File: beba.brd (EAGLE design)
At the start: 65 x 30 mm, 37 parts, among them IC1 LT1302SO08, IC2 MCP73871-2AAI/ML

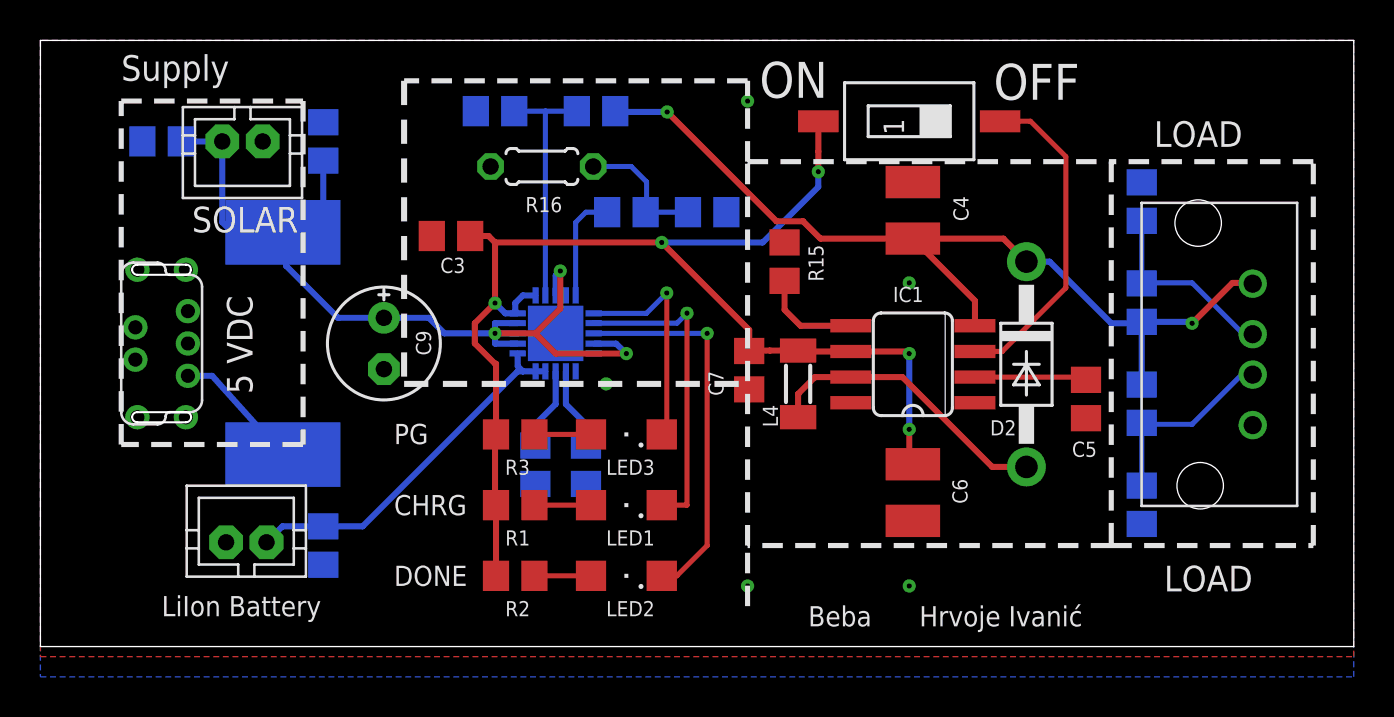
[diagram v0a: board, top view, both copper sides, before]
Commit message: - corrected issues with component placement, power inductor footprint, etc.
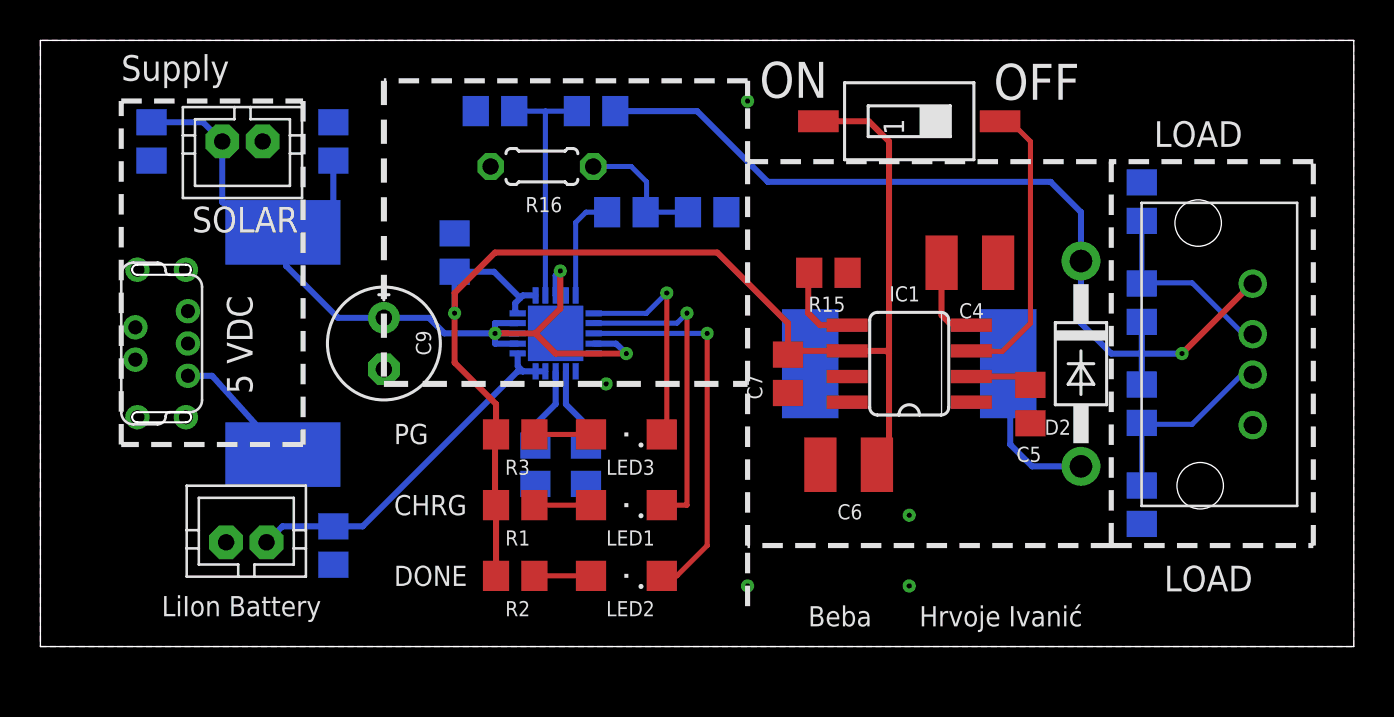
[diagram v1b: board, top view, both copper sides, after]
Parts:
- removed L4: DE1205-18, inductor-neosid:SM-1206
- added L: DE1205-18, DE1205-18 Power Inductor:SMT
- moved C4 3.83 mm to (46.0, 19.0), turned to 180 degrees
- moved C6 3.47 mm to (40.0, 9.00), turned to 0 degrees
- moved C5 2.76 mm to (49.0, 12.0)
- moved D2 2.70 mm to (51.5, 14.0)
- moved R15 2.24 mm to (39.0, 18.5), turned to 0 degrees
- moved C7 1.93 mm to (37.0, 13.5)
- moved C3 0.84 mm to (20.5, 19.5), flipped to the bottom, turned to 90 degrees
- moved C1 0.50 mm to (14.5, 5.00)
- moved C2 0.50 mm to (5.50, 25.0), turned to 270 degrees
- moved C8 0.50 mm to (14.5, 25.0)
- moved IC1 0.18 mm to (43.0, 14.0)
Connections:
- new net N$4: D2.A, L.L1
- net SW: no longer D2.A, L4.1
- net V_LIION_REGULATED: now also L.L2; no longer L4.2
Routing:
- net SW: track 14.6 -> 0.00 mm
- net N$4: track 0.00 -> 8.12 mm
- net V_LIION_REGULATED: track 62.9 -> 68.0 mm, vias 5 -> 1
- net VCC: track 45.5 -> 48.7 mm, vias 2 -> 1
- net 5V0: track 46.4 -> 48.9 mm
- net VC: track 5.55 -> 3.10 mm
- net SHDN: track 16.3 -> 14.4 mm
- net IT: track 5.04 -> 4.19 mm
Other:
- board text added: "+"
- board text added: "-"

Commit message: - further minor corrections
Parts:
- added 5V0, VLIION: PTR1B2,54, testpad:B2,54
- moved S1 2.06 mm to (45.0, 25.5)
- moved C1 0.71 mm to (14.0, 4.50)
- moved C2 0.71 mm to (5.00, 24.5)
- moved C3 0.71 mm to (20.0, 19.0)
- moved C4 0.71 mm to (45.5, 18.5)
- moved C5 0.71 mm to (48.5, 11.5)
- moved C6 0.71 mm to (39.5, 8.50)
- moved C7 0.71 mm to (36.5, 13.0)
- moved C8 0.71 mm to (14.0, 24.5)
- moved C9 0.71 mm to (16.5, 14.5)
- moved CONN1 0.71 mm to (5.50, 14.5)
- moved CONN2 0.71 mm to (9.69, 4.66)
- moved CONN3 0.71 mm to (9.50, 24.5)
- moved CONN4 0.71 mm to (59.5, 14.0)
- moved D2 0.71 mm to (51.0, 13.5)
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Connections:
- net 5V0: now also 5V0.TP
- net V_LIION_REGULATED: now also VLIION.TP
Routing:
- net 5V0: track 48.9 -> 61.6 mm
- net VCC: track 48.7 -> 52.8 mm, vias 1 -> 2
- net V_LIION_REGULATED: track 68.0 -> 69.1 mm
- net SHDN: track 14.4 -> 13.9 mm
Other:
- board size 65 x 30 mm -> 64 x 29.5 mm
- board text added: "Solar"
- board text removed: "SOLAR"

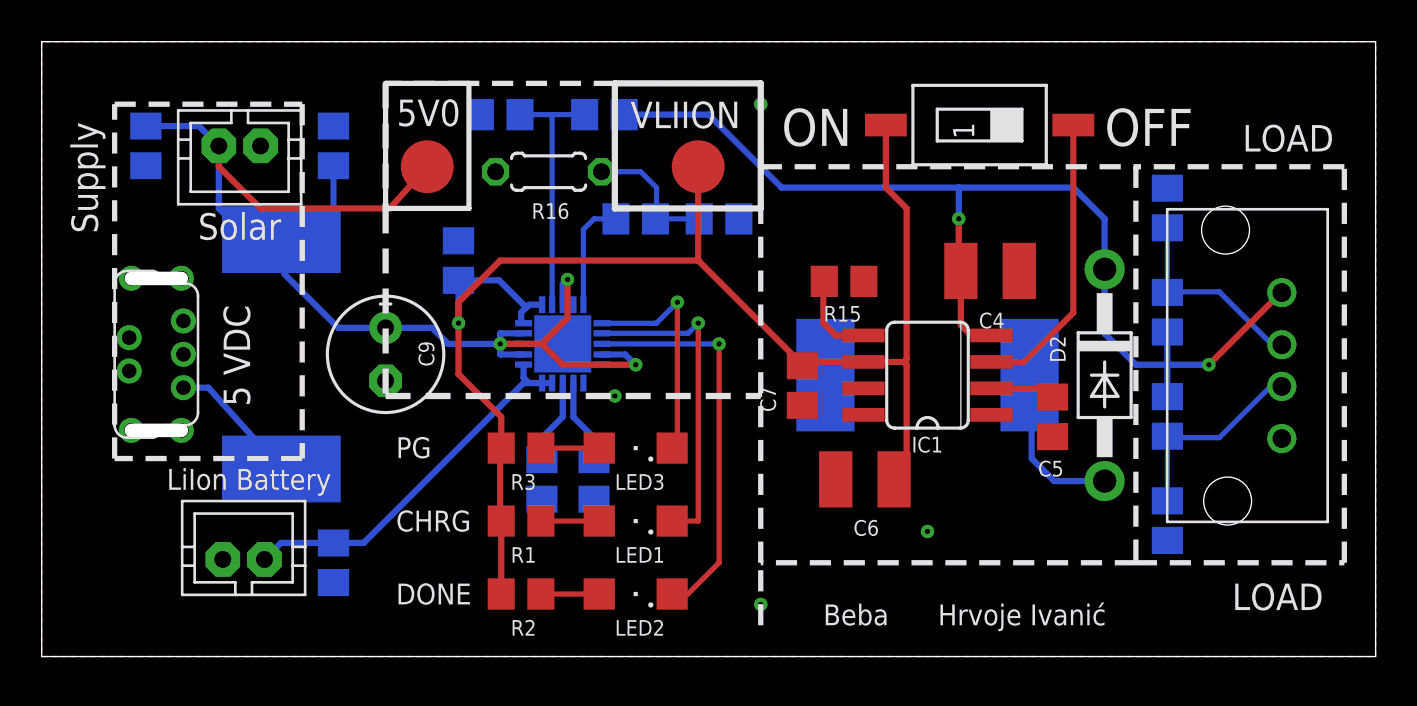
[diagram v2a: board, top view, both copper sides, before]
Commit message: - minor corrections, added bom
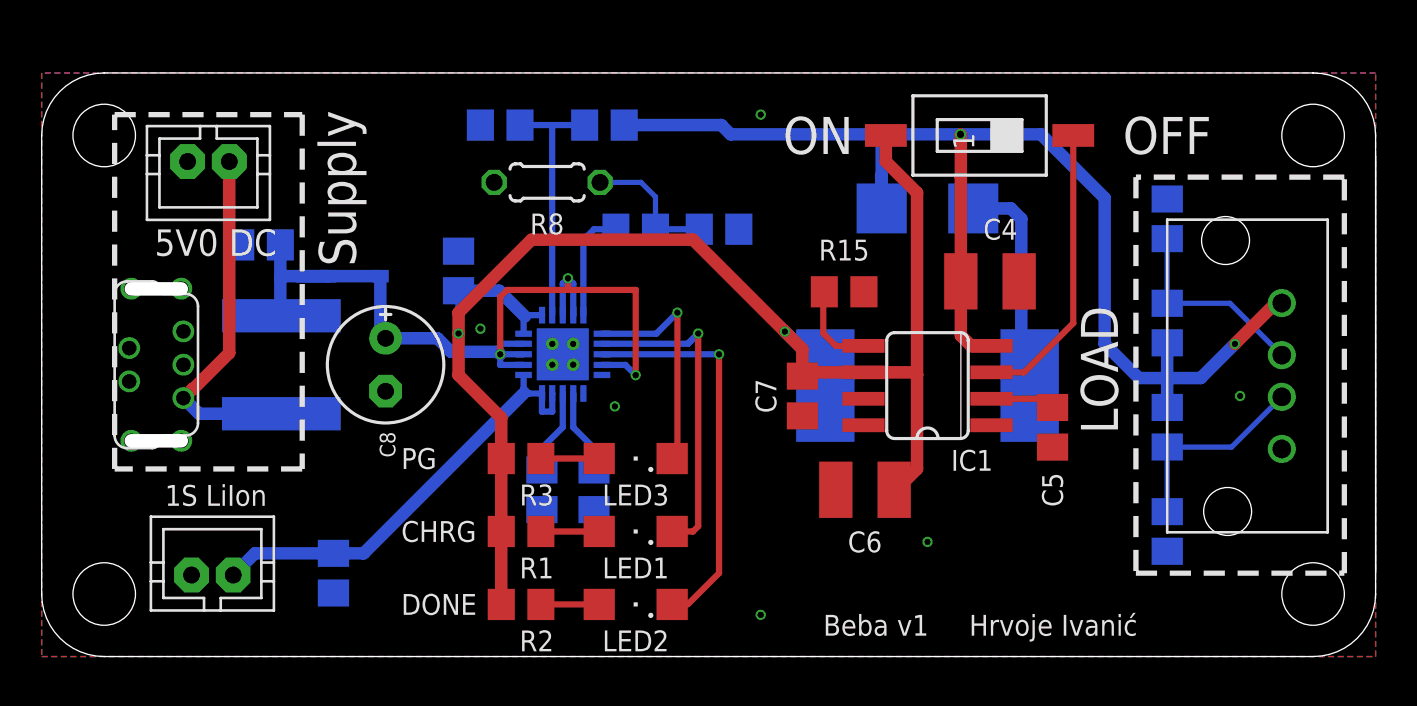
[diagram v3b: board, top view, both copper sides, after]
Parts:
- removed 5V0, VLIION: PTR1B2,54, testpad:B2,54
- removed C9: 4700μF / 10V, rcl:E2,5-6E
- removed L: DE1205-18, DE1205-18 Power Inductor:SMT
- removed R16: NTC - 10k, resistor:0204/5
- added D1: BAT60J, diode:SOD323_ST
- added L2: DE1205-18, DE1205-18 Power Inductor:SMT
- added R8: NTC - 10k, resistor:0204/5
- C8: value 10μF -> 4700μF / 10V; device resistor:C0805 -> rcl:E2,5-6E
- D2: value 1N4148 -> MBRS130LT3; device adafruit:DO41-10 -> diode:SMB
- IC2: device Microchip-MCP73871-2AAI_ML:QFN50P400X400X100-21N -> MCP73871 - Powerpath and Charge Controller:QFN50P400X400X100-21N
- moved D2 11.7 mm to (42.5, 21.5), flipped to the bottom, turned to 180 degrees
- moved C8 10.8 mm to (16.5, 14.0), flipped to the top, turned to 270 degrees
- moved C2 7.27 mm to (10.5, 19.8), turned to 0 degrees
- moved CONN2 1.68 mm to (8.19, 3.91)
- moved CONN3 1.68 mm to (8.00, 23.8)
- moved R11 0.52 mm to (54.0, 16.0)
- moved R12 0.52 mm to (54.0, 21.0)
- moved R13 0.52 mm to (54.0, 11.0)
- moved R14 0.52 mm to (54.0, 6.00)
- moved C1 0.50 mm to (14.0, 4.00)
- moved C3 0.50 mm to (20.0, 18.5)
- moved C4 0.50 mm to (45.5, 18.0)
- moved C5 0.50 mm to (48.5, 11.0)
- moved C6 0.50 mm to (39.5, 8.00)
- moved C7 0.50 mm to (36.5, 12.5)
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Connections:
- net 5V0: now also C8.+, D1.A, D1.C, IC2.17_CE, IC2.18_IN1, IC2.19_IN2, IC2.3_SEL, IC2.4_PROG2, IC2.9_!TE!, L1.1; no longer 5V0.TP, C8.1, C9.+, CONN3.1, IC2.17, IC2.18, IC2.19, IC2.3, IC2.4, IC2.9, L1.P$1
- net GND: now also C8.-, CONN3.1, IC2.10_GND1, IC2.11_GND2, IC2.GND2, IC2.GND3, IC2.GND4, IC2.GND5, IC2.GND6, R8.2; no longer C8.2, C9.-, CONN3.2, IC2.10, IC2.11, R16.2
- net N$10: now also R8.1; no longer R16.1
- net N$4: now also L2.L1; no longer L.L1
- net PG: now also IC2.!6_PG!; no longer IC2.6
- net PROG1: now also IC2.13_PROG1; no longer IC2.13
- net PROG3: now also IC2.12_PROG3; no longer IC2.12
- net STAT1: now also IC2.8_STAT1; no longer IC2.8
- net STAT2: now also IC2.7_STAT2; no longer IC2.7
- net THERM: now also IC2.5_THERM; no longer IC2.5
- net VPCC: now also IC2.2_VPCC; no longer IC2.2
- net VUSB: now also CONN3.2, L1.2; no longer L1.P$2
- net V_LIION+: now also IC2.14_VBAT1, IC2.15_VBAT2, IC2.16_BAT_SENSE; no longer IC2.14, IC2.15, IC2.16
- net V_LIION_REGULATED: now also IC2.1_OUT1, IC2.20_OUT2, L2.L2; no longer IC2.1, IC2.20, L.L2, VLIION.TP
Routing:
- net 5V0: track 61.6 -> 42.7 mm
- net VUSB: track 7.12 -> 17.3 mm
- net VCC: track 52.8 -> 62.0 mm
- net V_LIION+: track 18.3 -> 21.7 mm
- net N$4: track 8.12 -> 10.7 mm
- net V_LIION_REGULATED: track 69.1 -> 71.6 mm, vias 1 -> 2
- net GND: track 0.00 -> 0.71 mm, vias 4 -> 6
- net STAT2: track 15.6 -> 16.1 mm
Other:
- board size 64 x 29.5 mm -> 64 x 28 mm
- board text added: "1S LiIon"
- board text added: "5V0 DC"
- board text added: "Beba v1"
- board text removed: "+"
- board text removed: "-"
- board text removed: "5 VDC"
- board text removed: "Beba"
- board text removed: "LiIon Battery"
- board text removed: "Solar"

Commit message: - rewrote schematic into sheets
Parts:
- removed C1: 10uF, resistor:C0805
- removed C2, C3, C5: 10μF, resistor:C0805
- removed C4, C6: 220μF, resistor:C1210
- removed C7: 0.1μF, resistor:C0805
- removed C8: 4700μF / 10V, rcl:E2,5-6E
- removed CONN1: MX500075-1517USB_MINI-B, MX500075-1517 USB Mini-B straight socket:TH
- removed CONN2: LiIon, jst-ph:JST-PH2
- removed CONN3: 5VDC, jst-ph:JST-PH2
- removed CONN4: USB-A female socket, right angle, 1734366-1 USB-A socket, vertical:TH
- removed D1: BAT60J, diode:SOD323_ST
- removed D2: MBRS130LT3, diode:SMB
- removed IC1: LT1302SO08, adafruit:SO08
- removed IC2: MCP73871-2AAI/ML, MCP73871 - Powerpath and Charge Controller:QFN50P400X400X100-21N
- removed L1: DJNR6045-100-S, DJNR6045-100S Power Inductor:DJNR6045-100-S
- removed L2: DE1205-18, DE1205-18 Power Inductor:SMT
- removed LED1: green, led:SML1206
- removed LED2: orange, led:SML1206
- removed LED3: red, led:SML1206
- removed R10, R5: 100k, resistor:R0805
- removed R11, R13: 75k, resistor:R0805
- removed R12, R14: 49k9, resistor:R0805
- removed R15: 270k, resistor:R0805
- removed R6, R9: 1k, resistor:R0805
- removed R7: 150k, resistor:R0805
- removed R8: NTC - 10k, resistor:0204/5
- removed S1: POWER, smd-special:SMS-001
- added CN1, CN2, CN3: S2B-PH-K-S, adafruit:JST-PH-2-THM-RA
- added IDEAL_DIODE1:C1, IDEAL_DIODE2:C1, IDEAL_DIODE3:C1, TPS630701-1:C11: 0.1μF, rcl:C0805
- added IDEAL_DIODE1:IC1, IDEAL_DIODE2:IC1, IDEAL_DIODE3:IC1: SIA456DJ-T1-GE3, SIA456DJ-T1-GE3 N-Fet:SC-70-6
- added IDEAL_DIODE1:IC2, IDEAL_DIODE2:IC2, IDEAL_DIODE3:IC2: LM74670QDGKTQ1, LM74670 - Smart Diode Rectifier Controller:VSSOP-8
- added MCP73871-1:C16: 4700μF / 10V, C-Pol:TH
- added MCP73871-1:C4: 10μF, resistor:C0805
- added MCP73871-1:C6, MCP73871-1:C7: 10u, resistor:C0805
- added MCP73871-1:IC7: (no value), MCP73871 - Powerpath and Charge Controller:QFN50P400X400X100-21N
- added MCP73871-1:LED1: LTST-C230KRKT - red, led:SML1206
- added MCP73871-1:LED2: LTST-C230KGKT - green, led:SML1206
- added MCP73871-1:LED3: LTST-C230KSKT - yellow, led:SML1206
- added MCP73871-1:R1, MCP73871-1:R2, MCP73871-1:R3, MCP73871-1:R6, MCP73871-1:R7: 1k, resistor:R0805
- added MCP73871-1:R10: NTC - 10k, resistor:0204/5
- added MCP73871-1:R4: 270k, resistor:R0805
- added MCP73871-1:R5, MCP73871-1:R8: 100k, resistor:R0805
- added MCP73871-1:R9: 150k, resistor:R0805
- added TPS630701-1:C10, TPS630701-1:C12, TPS630701-1:C8, TPS630701-1:C9: 10u, rcl:C0805
- added TPS630701-1:C13, TPS630701-1:C14, TPS630701-1:C15: 22u, rcl:C0805
- added TPS630701-1:IC8: TPS630701, TPS630701 - Buck Boost 5V regulator:VQFN
- added TPS630701-1:L1: XFL4020-152MEB, XFL4020-152MEC Inductor 1.5uH:SMD
- added TPS630701-1:R11: 100k, rcl:R0805
- added TPS630701-1:R12: 10k, rcl:R0805
- added USB-B1: 67503-1230, MX-67503-1230 USB Mini-B SMT straight socket:SMT
- added X1: 62900416021, con-yamaichi:USB-A003
- R1, R3: value 1k -> 75k
- R2: value 1k -> 49k9
- R4: value 270k -> 49k9
- moved R4 252.9 mm to (-95.0, -196.0), flipped to the top, turned to 0 degrees
- moved R3 243.6 mm to (-96.0, -203.0)
- moved R1 243.0 mm to (-101.0, -203.0)
- moved R2 234.0 mm to (-101.0, -196.0)
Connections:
- removed net 5V0: C2.1, C8.+, D1.A, D1.C, IC2.17_CE, IC2.18_IN1, IC2.19_IN2, IC2.3_SEL, IC2.4_PROG2, IC2.9_!TE!, L1.1
- removed net IT: IC1.5, R15.1
- removed net N$1: LED3.A, R3.2
- removed net N$10: R6.2, R7.1, R8.1
- removed net N$2: LED2.A, R2.2
- removed net N$3: LED1.A, R1.2
- removed net N$4: D2.A, L2.L1
- removed net PG: IC2.!6_PG!, LED3.C
- removed net PROG1: IC2.13_PROG1, R9.1
- removed net PROG3: IC2.12_PROG3, R10.1
- removed net SHDN: IC1.3, S1.2
- removed net STAT1: IC2.8_STAT1, LED2.C
- removed net STAT2: IC2.7_STAT2, LED1.C
- removed net SW: IC1.7
- removed net THERM: IC2.5_THERM, R6.1
- removed net VC: C5.2, IC1.2
- removed net VCC: C4.2, CONN4.VCC, D2.C, IC1.4, R11.2, R13.2, R4.2
- removed net VPCC: IC2.2_VPCC, R4.1, R5.2
- removed net VUSB: CONN1.VBUS, CONN3.2, L1.2
- new net 5V0_IN: IDEAL_DIODE1:IC1.1_D, IDEAL_DIODE1:IC1.2_D, IDEAL_DIODE1:IC1.5_D, IDEAL_DIODE1:IC1.6_D, IDEAL_DIODE1:IC1.8_D, IDEAL_DIODE1:IC2.CATHODE, IDEAL_DIODE2:IC1.1_D, IDEAL_DIODE2:IC1.2_D, IDEAL_DIODE2:IC1.5_D, IDEAL_DIODE2:IC1.6_D, IDEAL_DIODE2:IC1.8_D, IDEAL_DIODE2:IC2.CATHODE, IDEAL_DIODE3:IC1.1_D, IDEAL_DIODE3:IC1.2_D, IDEAL_DIODE3:IC1.5_D, IDEAL_DIODE3:IC1.6_D, IDEAL_DIODE3:IC1.8_D, IDEAL_DIODE3:IC2.CATHODE
- new net 5V0_OUT: R1.2, R3.2, X1.1
- new net IDEAL_DIODE1:GATE_DRIVER: IDEAL_DIODE1:IC1.3_G, IDEAL_DIODE1:IC2.GATE_DRIVE, IDEAL_DIODE1:IC2.GATE_PULLD
- new net IDEAL_DIODE1:VCAPH: IDEAL_DIODE1:C1.2, IDEAL_DIODE1:IC2.VCAPH
- new net IDEAL_DIODE1:VCAPL: IDEAL_DIODE1:C1.1, IDEAL_DIODE1:IC2.VCAPL
- new net IDEAL_DIODE2:GATE_DRIVER: IDEAL_DIODE2:IC1.3_G, IDEAL_DIODE2:IC2.GATE_DRIVE, IDEAL_DIODE2:IC2.GATE_PULLD
- new net IDEAL_DIODE2:VCAPH: IDEAL_DIODE2:C1.2, IDEAL_DIODE2:IC2.VCAPH
- new net IDEAL_DIODE2:VCAPL: IDEAL_DIODE2:C1.1, IDEAL_DIODE2:IC2.VCAPL
- new net IDEAL_DIODE3:GATE_DRIVER: IDEAL_DIODE3:IC1.3_G, IDEAL_DIODE3:IC2.GATE_DRIVE, IDEAL_DIODE3:IC2.GATE_PULLD
- new net IDEAL_DIODE3:VCAPH: IDEAL_DIODE3:C1.2, IDEAL_DIODE3:IC2.VCAPH
- new net IDEAL_DIODE3:VCAPL: IDEAL_DIODE3:C1.1, IDEAL_DIODE3:IC2.VCAPL
- new net MCP73871-1:5V0_IN: MCP73871-1:C16.POS, MCP73871-1:C4.1, MCP73871-1:IC7.17_CE, MCP73871-1:IC7.18_IN1, MCP73871-1:IC7.19_IN2, MCP73871-1:IC7.3_SEL, MCP73871-1:IC7.4_PROG2, MCP73871-1:IC7.9_!TE!, MCP73871-1:R1.1, MCP73871-1:R2.1, MCP73871-1:R3.1, MCP73871-1:R4.2
- new net MCP73871-1:LED1_A: MCP73871-1:LED1.A, MCP73871-1:R1.2
- new net MCP73871-1:LED2_A: MCP73871-1:LED2.A, MCP73871-1:R2.2
- new net MCP73871-1:LED3_A: MCP73871-1:LED3.A, MCP73871-1:R3.2
- new net MCP73871-1:N$10: MCP73871-1:R10.1, MCP73871-1:R6.2, MCP73871-1:R9.1
- new net MCP73871-1:PG: MCP73871-1:IC7.!6_PG!, MCP73871-1:LED1.C
- new net MCP73871-1:PROG1: MCP73871-1:IC7.13_PROG1, MCP73871-1:R7.1
- new net MCP73871-1:PROG3: MCP73871-1:IC7.12_PROG3, MCP73871-1:R8.1
- new net MCP73871-1:STAT1: MCP73871-1:IC7.8_STAT1/!LBO!, MCP73871-1:LED3.C
- new net MCP73871-1:STAT2: MCP73871-1:IC7.7_STAT2, MCP73871-1:LED2.C
- new net MCP73871-1:THERM: MCP73871-1:IC7.5_THERM, MCP73871-1:R6.1
- new net MCP73871-1:VPCC: MCP73871-1:IC7.2_VPCC, MCP73871-1:R4.1, MCP73871-1:R5.2
- new net MCP73871-1:V_LIION+: MCP73871-1:C7.1, MCP73871-1:IC7.14_VBAT1, MCP73871-1:IC7.15_VBAT2, MCP73871-1:IC7.16_BAT_SENSE
- new net MCP73871-1:V_LIION_REGULATED: MCP73871-1:C6.1, MCP73871-1:IC7.1_OUT1, MCP73871-1:IC7.20_OUT2
- new net TPS630701-1:5V0_OUT: TPS630701-1:C12.2, TPS630701-1:C13.2, TPS630701-1:C14.2, TPS630701-1:C15.2, TPS630701-1:IC8.5-FB, TPS630701-1:IC8.7-VOUT, TPS630701-1:IC8.8-VOUT, TPS630701-1:IC8.VOUT, TPS630701-1:R11.2
- new net TPS630701-1:L1: TPS630701-1:IC8.11-L1, TPS630701-1:L1.P$1
- new net TPS630701-1:L2: TPS630701-1:IC8.9-L2, TPS630701-1:L1.P$2
- new net TPS630701-1:N$8: TPS630701-1:IC8.1-PS/S, TPS630701-1:IC8.14-EN, TPS630701-1:R12.1
- new net TPS630701-1:PG1: TPS630701-1:IC8.2-PG, TPS630701-1:R11.1
- new net TPS630701-1:VAUX: TPS630701-1:C11.2, TPS630701-1:IC8.3-VAUX
- new net VINPUT1: CN1.1, IDEAL_DIODE2:IC1.4_S, IDEAL_DIODE2:IC1.7_S, IDEAL_DIODE2:IC2.ANODE
- new net VINPUT2: CN2.1, IDEAL_DIODE3:IC1.4_S, IDEAL_DIODE3:IC1.7_S, IDEAL_DIODE3:IC2.ANODE
- new net VUSB_MINI-B: IDEAL_DIODE1:IC1.4_S, IDEAL_DIODE1:IC1.7_S, IDEAL_DIODE1:IC2.ANODE, USB-B1.VBUS
- net GND: now also CN1.2, CN2.2, CN3.2, MCP73871-1:C16.NEG, MCP73871-1:C4.2, MCP73871-1:C6.2, MCP73871-1:C7.2, MCP73871-1:IC7.10_GND1, MCP73871-1:IC7.11_GND2, MCP73871-1:IC7.GND2, MCP73871-1:IC7.GND3, MCP73871-1:IC7.GND4, MCP73871-1:IC7.GND5, MCP73871-1:IC7.GND6, MCP73871-1:R10.2, MCP73871-1:R5.1, MCP73871-1:R7.2, MCP73871-1:R8.2, MCP73871-1:R9.2, R2.1, R4.1, TPS630701-1:C10.1, TPS630701-1:C11.1, TPS630701-1:C12.1, TPS630701-1:C13.1, TPS630701-1:C14.1, TPS630701-1:C15.1, TPS630701-1:C8.1, TPS630701-1:C9.1, TPS630701-1:IC8.10-PGND, TPS630701-1:IC8.15-VSEL, TPS630701-1:IC8.4-GND, TPS630701-1:IC8.6-FB2, USB-B1.GND1, USB-B1.GND2, USB-B1.GND3, USB-B1.GND4, USB-B1.GND5, X1.4; no longer C1.2, C2.2, C3.2, C4.1, C5.1, C6.1, C7.1, C8.-, CONN1.GND1, CONN2.2, CONN3.1, CONN4.GND, IC1.1, IC1.8, IC2.10_GND1, IC2.11_GND2, IC2.GND2, IC2.GND3, IC2.GND4, IC2.GND5, IC2.GND6, R10.2, R12.1, R14.1, R15.2, R5.1, R7.2, R8.2, R9.2
- net USBDN: now also R1.1, R2.2, X1.2; no longer CONN4.USBDN, R11.1, R12.2
- net USBDP: now also R3.1, R4.2, X1.3; no longer CONN4.USBDP, R13.1, R14.2
- net V_LIION+: now also CN3.1; no longer C1.1, CONN2.1, IC2.14_VBAT1, IC2.15_VBAT2, IC2.16_BAT_SENSE
- net V_LIION_REGULATED: now also TPS630701-1:C10.2, TPS630701-1:C8.2, TPS630701-1:C9.2, TPS630701-1:IC8.12-VIN, TPS630701-1:IC8.13-VIN, TPS630701-1:IC8.VIN, TPS630701-1:R12.2; no longer C3.1, C6.2, C7.2, IC1.6, IC2.1_OUT1, IC2.20_OUT2, L2.L2, R1.1, R2.1, R3.1, S1.1
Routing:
- net V_LIION_REGULATED: track 71.6 -> 0.00 mm, vias 2 -> 3
- net VCC: track 62.0 -> 0.00 mm, vias 2 -> 0
- net 5V0: track 42.7 -> 0.00 mm, vias 3 -> 0
- net V_LIION+: track 21.7 -> 0.00 mm
- net STAT1: track 19.0 -> 0.00 mm, vias 1 -> 0
- net VUSB: track 17.3 -> 0.00 mm
- net STAT2: track 16.1 -> 0.00 mm, vias 1 -> 0
- net SHDN: track 13.9 -> 0.00 mm
- net VPCC: track 12.2 -> 0.00 mm
- net PG: track 11.2 -> 0.00 mm, vias 1 -> 0
- net N$4: track 10.7 -> 0.00 mm
- net VINPUT1: track 0.00 -> 10.0 mm, vias 0 -> 1
- net VINPUT2: track 0.00 -> 10.0 mm, vias 0 -> 1
- net N$10: track 6.60 -> 0.00 mm
- net USBDN: track 9.63 -> 3.05 mm, vias 0 -> 1
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- added copper zone on layer 1, net 5V0_IN
- added copper zone on layer 1, net 5V0_OUT
- added copper zone on layer 16, net 5V0_OUT
- added copper zone on layer 1, net L1
- added copper zone on layer 1, net L2
- added copper zone on layer 1, net V_LIION+
- added copper zone on layer 1, net V_LIION_REGULATED
- added copper zone on layer 16, net V_LIION_REGULATED
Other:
- board size 64 x 28 mm -> 77 x 20 mm
- board text removed: "1S LiIon"
- board text removed: "5V0 DC"
- board text removed: "Beba v1"
- board text removed: "CHRG"
- board text removed: "DONE"
- board text removed: "Hrvoje Ivanić"
- board text removed: "LOAD"
- board text removed: "OFF"
- board text removed: "ON"
- board text removed: "PG"
- board text removed: "Supply"
